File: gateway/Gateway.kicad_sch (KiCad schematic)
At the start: 0 parts

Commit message: Working on first version
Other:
- note added: "Revision: ${REVISION}"
- note removed: "Rev ${REVISION}"
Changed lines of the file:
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@@
 			(font
 				(face "Times New Roman")
-				(size 11 11)
+				(size 8 8)
 				(thickness 1)
 				(bold yes)
@@
 		)
 	)
-	(text "Rev ${REVISION}"
+	(text "Revision: ${REVISION}"
 		(exclude_from_sim no)
 		(at 394.97 59.69 0)
@@
 			(font
 				(face "Times New Roman")
-				(size 11 11)
+				(size 8 8)
 				(thickness 1)
 				(bold yes)

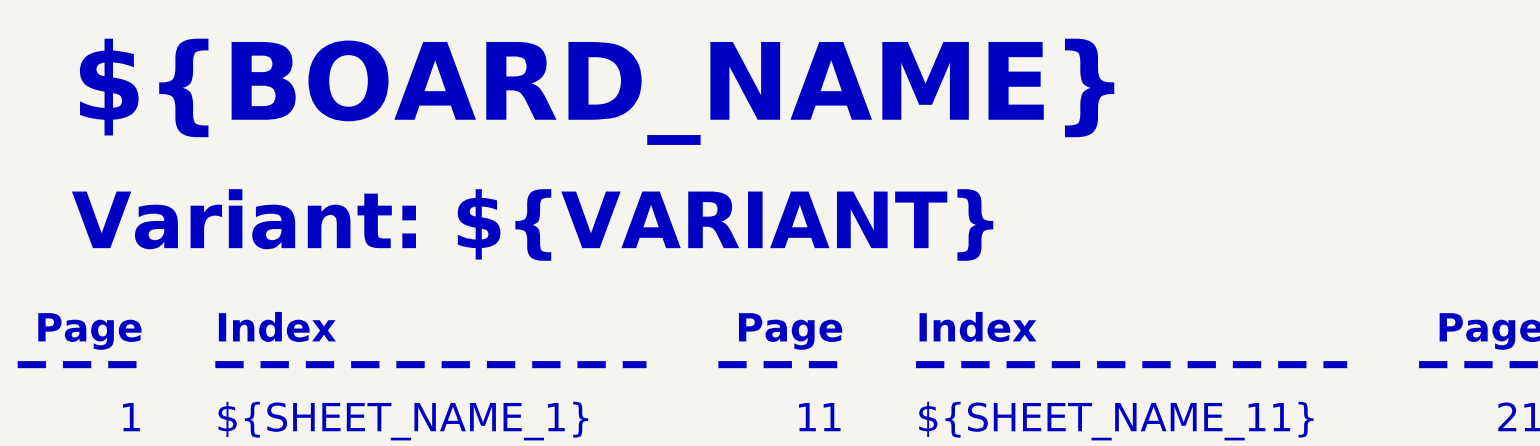
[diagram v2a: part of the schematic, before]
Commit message: Fix broken variant variable
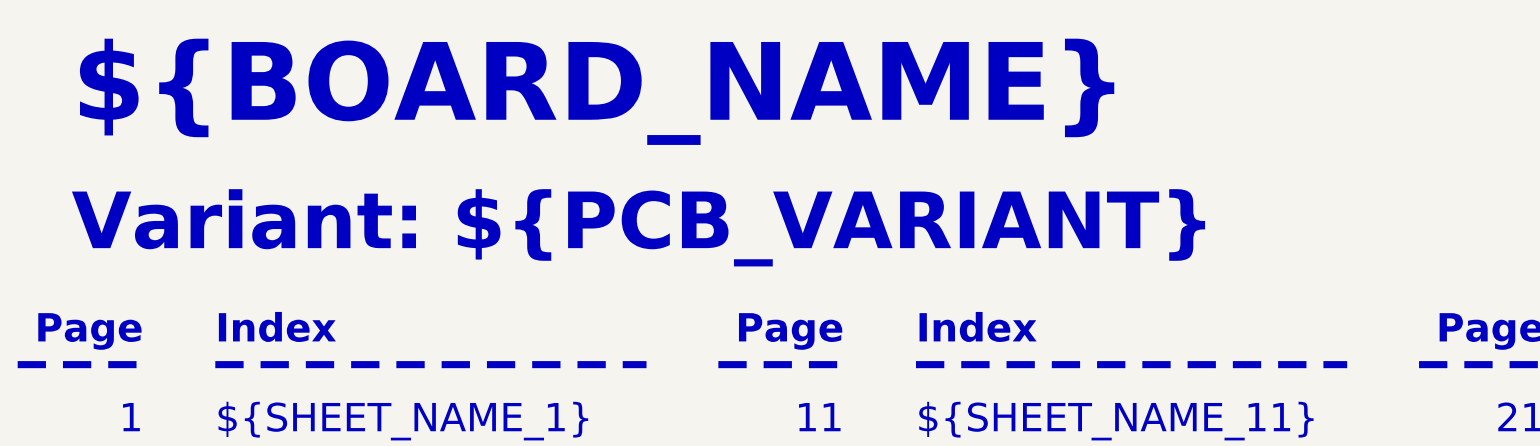
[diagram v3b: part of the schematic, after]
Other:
- note added: "Variant: ${PCB_VARIANT}"
- note removed: "Variant: ${VARIANT}"
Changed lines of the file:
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@@
 		(company "${COMPANY}")
 	)
-	(text "Variant: ${VARIANT}"
+	(text "Variant: ${PCB_VARIANT}"
 		(exclude_from_sim no)
 		(at 31.75 59.69 0)
